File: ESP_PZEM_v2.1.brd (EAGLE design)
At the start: 74 x 30 mm, 31 parts, among them IC1 ESP01S, IC3 74HC4052D, Q1 BSS138, Q2 BSS138, U1 LM1117-3.3, X1 KF301-5.0-2P, X2 S4B-XH-A-1, X3 S4B-XH-A-1, X4 S4B-XH-A-1, X5 S4B-XH-A-1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

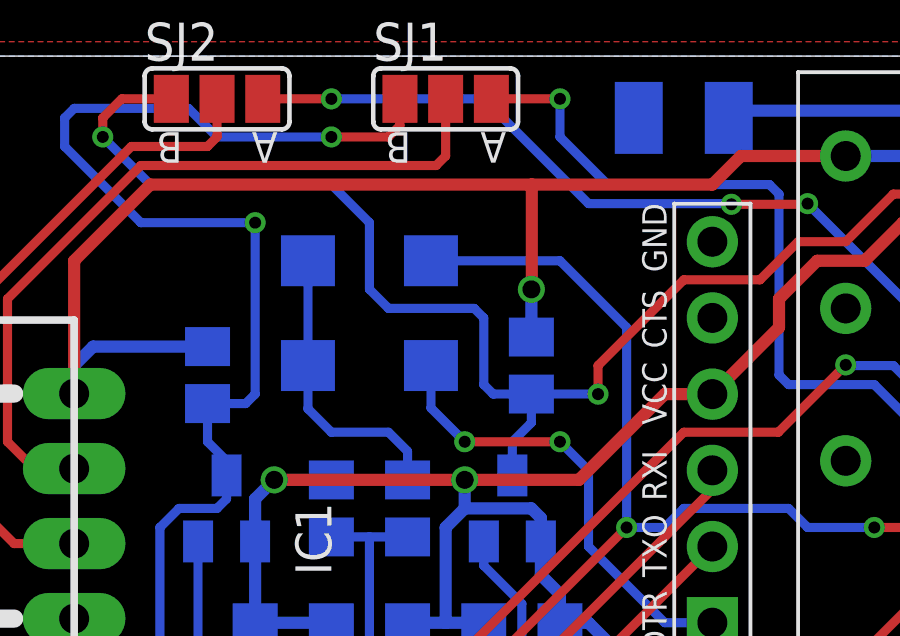
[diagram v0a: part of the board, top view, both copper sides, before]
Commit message: SS16 -> BAT54C
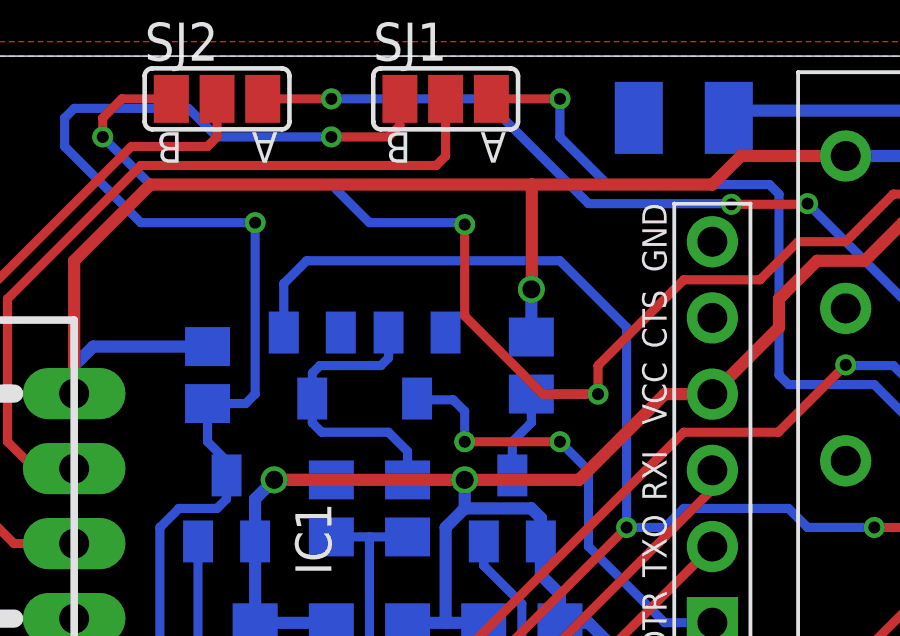
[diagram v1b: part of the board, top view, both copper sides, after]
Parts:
- D1, D2: value SS16 -> BAT54C; device my-diode:DO214AC -> diode:SOT23
- moved D2 3.98 mm to (15.2, 19.7)
- moved D1 1.59 mm to (18.7, 19.7), turned to 180 degrees
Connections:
- net N$2: now also D1.1, D2.3; no longer D1.A, D2.C
- net N$8: now also D1.3; no longer D1.C
- net S0: now also D2.1; no longer D2.A
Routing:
- net S0: track 49.7 -> 56.6 mm
- net RX_IN: track 57.5 -> 58.9 mm, vias 3 -> 4

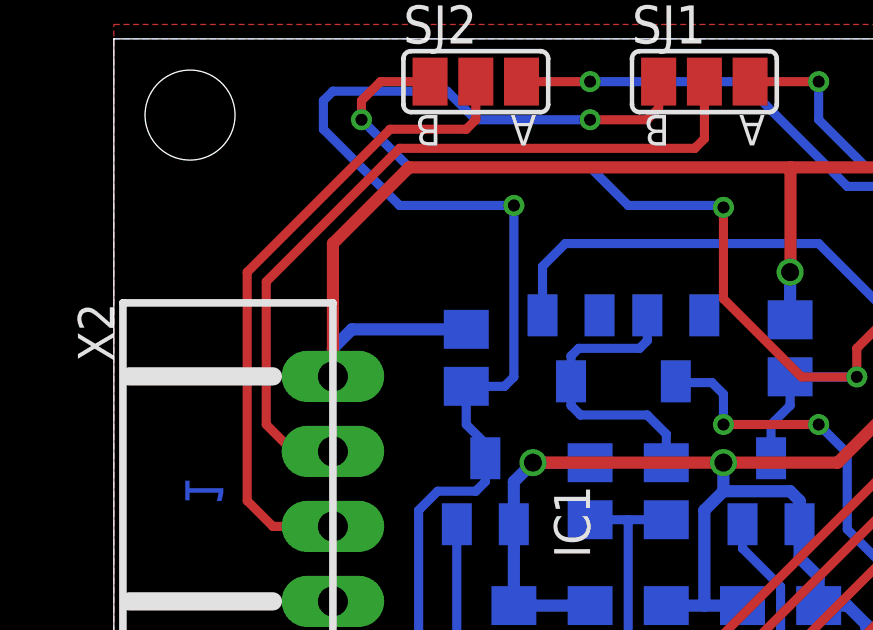
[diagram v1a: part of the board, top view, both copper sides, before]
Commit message: resistor moved
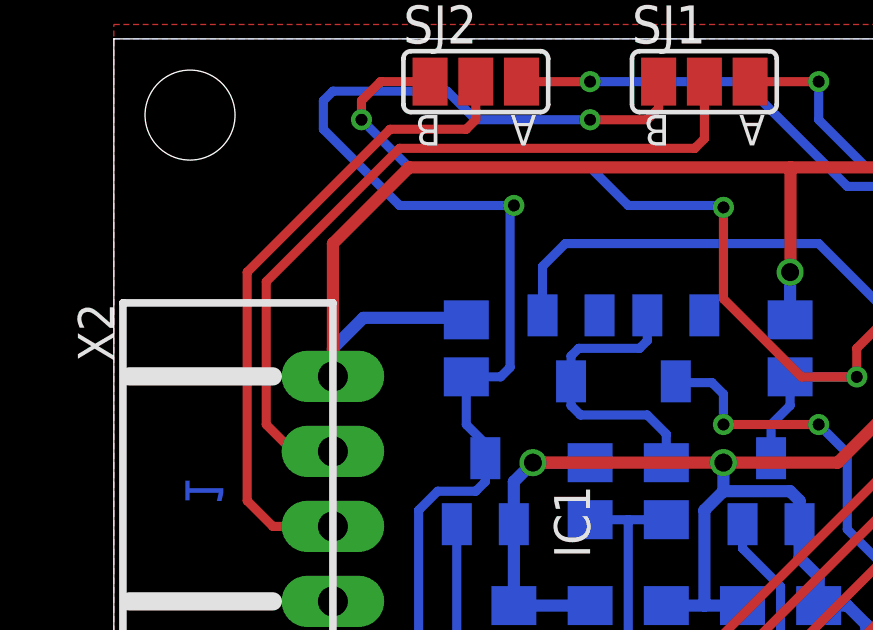
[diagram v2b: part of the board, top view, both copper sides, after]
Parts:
- moved R6 0.32 mm to (11.7, 19.7)
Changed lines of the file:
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@@
 <attribute name="VALUE" x="18.415" y="11.43" size="0.8" layer="28" font="vector" rot="MR270" align="center-right"/>
 </element>
-<element name="R6" library="rcl" library_urn="urn:adsk.eagle:library:334" package="R0805" package3d_urn="urn:adsk.eagle:package:23553/2" value="10K" x="11.7475" y="19.3675" smashed="yes" rot="MR90">
-<attribute name="NAME" x="10.795" y="19.3675" size="1.2" layer="26" font="vector" rot="MR270" align="bottom-center"/>
-<attribute name="SPICEPREFIX" value="R" x="11.7475" y="19.3675" size="1.778" layer="28" rot="MR90" display="off"/>
-<attribute name="VALUE" x="11.7475" y="20.6375" size="0.8" layer="28" font="vector" rot="MR270" align="center-right"/>
+<element name="R6" library="rcl" library_urn="urn:adsk.eagle:library:334" package="R0805" package3d_urn="urn:adsk.eagle:package:23553/2" value="10K" x="11.7475" y="19.685" smashed="yes" rot="MR90">
+<attribute name="NAME" x="10.795" y="19.685" size="1.2" layer="26" font="vector" rot="MR270" align="bottom-center"/>
+<attribute name="SPICEPREFIX" value="R" x="11.7475" y="19.685" size="1.778" layer="28" rot="MR90" display="off"/>
+<attribute name="VALUE" x="11.7475" y="20.955" size="0.8" layer="28" font="vector" rot="MR270" align="center-right"/>
 </element>
 <element name="R7" library="rcl" library_urn="urn:adsk.eagle:library:334" package="R0805" package3d_urn="urn:adsk.eagle:package:23553/2" value="10K" x="22.5425" y="19.685" smashed="yes" rot="MR90">
@@
 <wire x1="12.3825" y1="16.0225" x2="12.3825" y2="16.51" width="0.3048" layer="16"/>
 <wire x1="12.3825" y1="16.51" x2="11.7475" y2="17.145" width="0.3048" layer="16"/>
-<wire x1="11.7475" y1="17.145" x2="11.7475" y2="18.4175" width="0.3048" layer="16"/>
-<wire x1="13.335" y1="18.7325" x2="13.335" y2="24.4475" width="0.3048" layer="16"/>
+<wire x1="11.7475" y1="17.145" x2="11.7475" y2="18.735" width="0.3048" layer="16"/>
 <via x="13.335" y="24.4475" extent="1-16" drill="0.4"/>
 <via x="15.875" y="27.305" extent="1-16" drill="0.4"/>
@@
 <wire x1="12.3825" y1="15.24" x2="12.3825" y2="16.0225" width="0.3048" layer="16"/>
 <wire x1="38.4175" y1="5.3975" x2="34.6075" y2="1.5875" width="0.3048" layer="16"/>
-<wire x1="11.7475" y1="18.4175" x2="13.02" y2="18.4175" width="0.3048" layer="16"/>
-<wire x1="13.02" y1="18.4175" x2="13.335" y2="18.7325" width="0.3048" layer="16"/>
+<wire x1="13.335" y1="24.4475" x2="13.208" y2="24.3205" width="0.3048" layer="16"/>
+<wire x1="12.893" y1="18.735" x2="11.7475" y2="18.735" width="0.3048" layer="16"/>
+<wire x1="13.208" y1="24.3205" x2="13.208" y2="19.05" width="0.3048" layer="16"/>
+<wire x1="13.208" y1="19.05" x2="12.893" y2="18.735" width="0.3048" layer="16"/>
 </signal>
 <signal name="RX_IN">
@@
 <wire x1="37.6936" y1="26.1239" x2="44.3611" y2="26.1239" width="0.4064" layer="16"/>
 <wire x1="47.625" y1="22.86" x2="47.625" y2="17.9959" width="0.4064" layer="16"/>
-<wire x1="11.7475" y1="20.3175" x2="7.935" y2="20.3175" width="0.4064" layer="16"/>
-<wire x1="7.935" y1="20.3175" x2="7.3025" y2="19.685" width="0.4064" layer="16"/>
+<wire x1="11.7475" y1="20.635" x2="11.6815" y2="20.701" width="0.4064" layer="16"/>
+<wire x1="11.6815" y1="20.701" x2="8.3185" y2="20.701" width="0.4064" layer="16"/>
+<wire x1="8.3185" y1="20.701" x2="7.3025" y2="19.685" width="0.4064" layer="16"/>
 </signal>
 <signal name="N$1">
